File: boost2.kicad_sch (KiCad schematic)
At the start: 21 parts, among them IC1 CSD18543Q3A, IC2 LM3481QMMX_NOPB

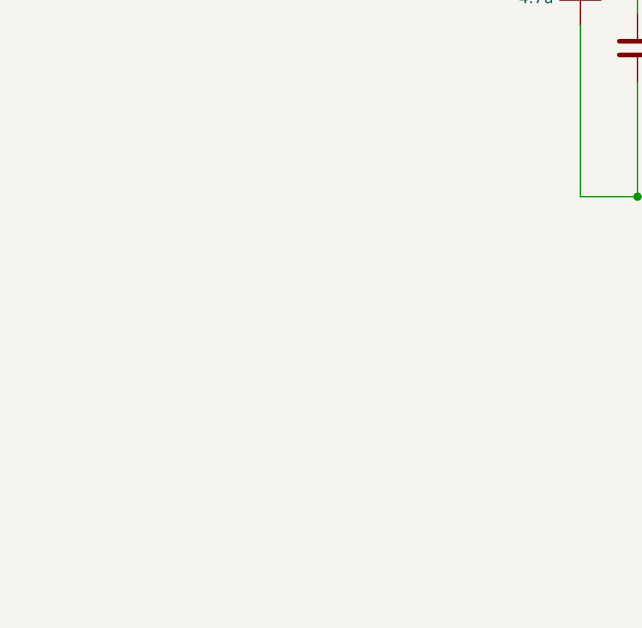
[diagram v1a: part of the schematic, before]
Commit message: Add new boost converter to boost2 subsheet
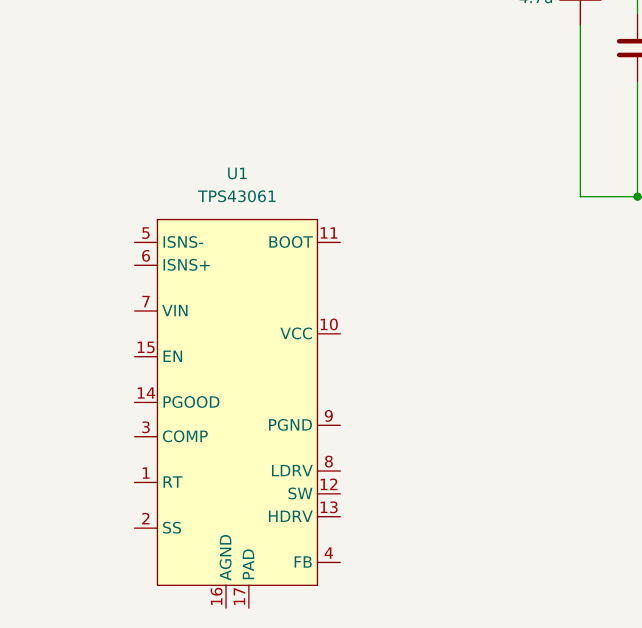
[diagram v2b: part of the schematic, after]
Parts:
- added U1: TPS43061, ! Robomaster ICs:Texas_S-PWQFN-N16, symbol ! Robomaster ICs:TPS43061
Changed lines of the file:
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@@
+	)
+	(symbol
+		(lib_id "! Robomaster ICs:TPS43061")
+		(at 48.26 138.43 0)
+		(unit 1)
+		(exclude_from_sim no)
+		(in_bom yes)
+		(on_board yes)
+		(dnp no)
+		(fields_autoplaced yes)
+		(property "Reference" "U1"
+			(at 48.26 133.35 0)
+			(effects
+				(font
+					(size 1.27 1.27)
+				)
+			)
+		)
+		(property "Value" "TPS43061"
+			(at 48.26 135.89 0)
+			(effects
+				(font
+					(size 1.27 1.27)
+				)
+			)
+		)
+		(property "Footprint" "! Robomaster ICs:Texas_S-PWQFN-N16"
+			(at 48.26 138.43 0)
+			(effects
+				(font
+					(size 1.27 1.27)
+				)
+				(hide yes)
+			)
+		)
+		(property "Datasheet" "https://www.ti.com/lit/ds/symlink/tps43061.pdf"
+			(at 48.26 138.43 0)
+			(effects
+				(font
+					(size 1.27 1.27)
+				)
+				(hide yes)
+			)
+		)
+		(property "Description" "Low Iq, Synchronous Boost Controller with Wide Input Voltage and 5.5V Gate Drive for Low Qg NexFETs"
+			(at 48.26 138.43 0)
+			(effects
+				(font
+					(size 1.27 1.27)
+				)
+				(hide yes)
+			)
+		)
+		(pin "11"
+		)
+		(pin "8"
+		)
+		(pin "12"
+		)
+		(pin "7"
+		)
+		(pin "6"
+		)
+		(pin "4"
+		)
+		(pin "13"
+		)
+		(pin "2"
+		)
+		(pin "16"
+		)
+		(pin "14"
+		)
+		(pin "17"
+		)
+		(pin "3"
+		)
+		(pin "9"
+		)
+		(pin "5"
+		)
+		(pin "10"
+		)
+		(pin "15"
+		)
+		(pin "1"
+		)
+		(instances
+			(project ""
+				(path "/6197145b-e7d4-44cc-9d90-537b6501bf60/47dffa6f-2678-4be2-969a-7f2e7310ccad"
+					(reference "U1")
+					(unit 1)
+				)
+			)
+		)
 	)
 	(symbol

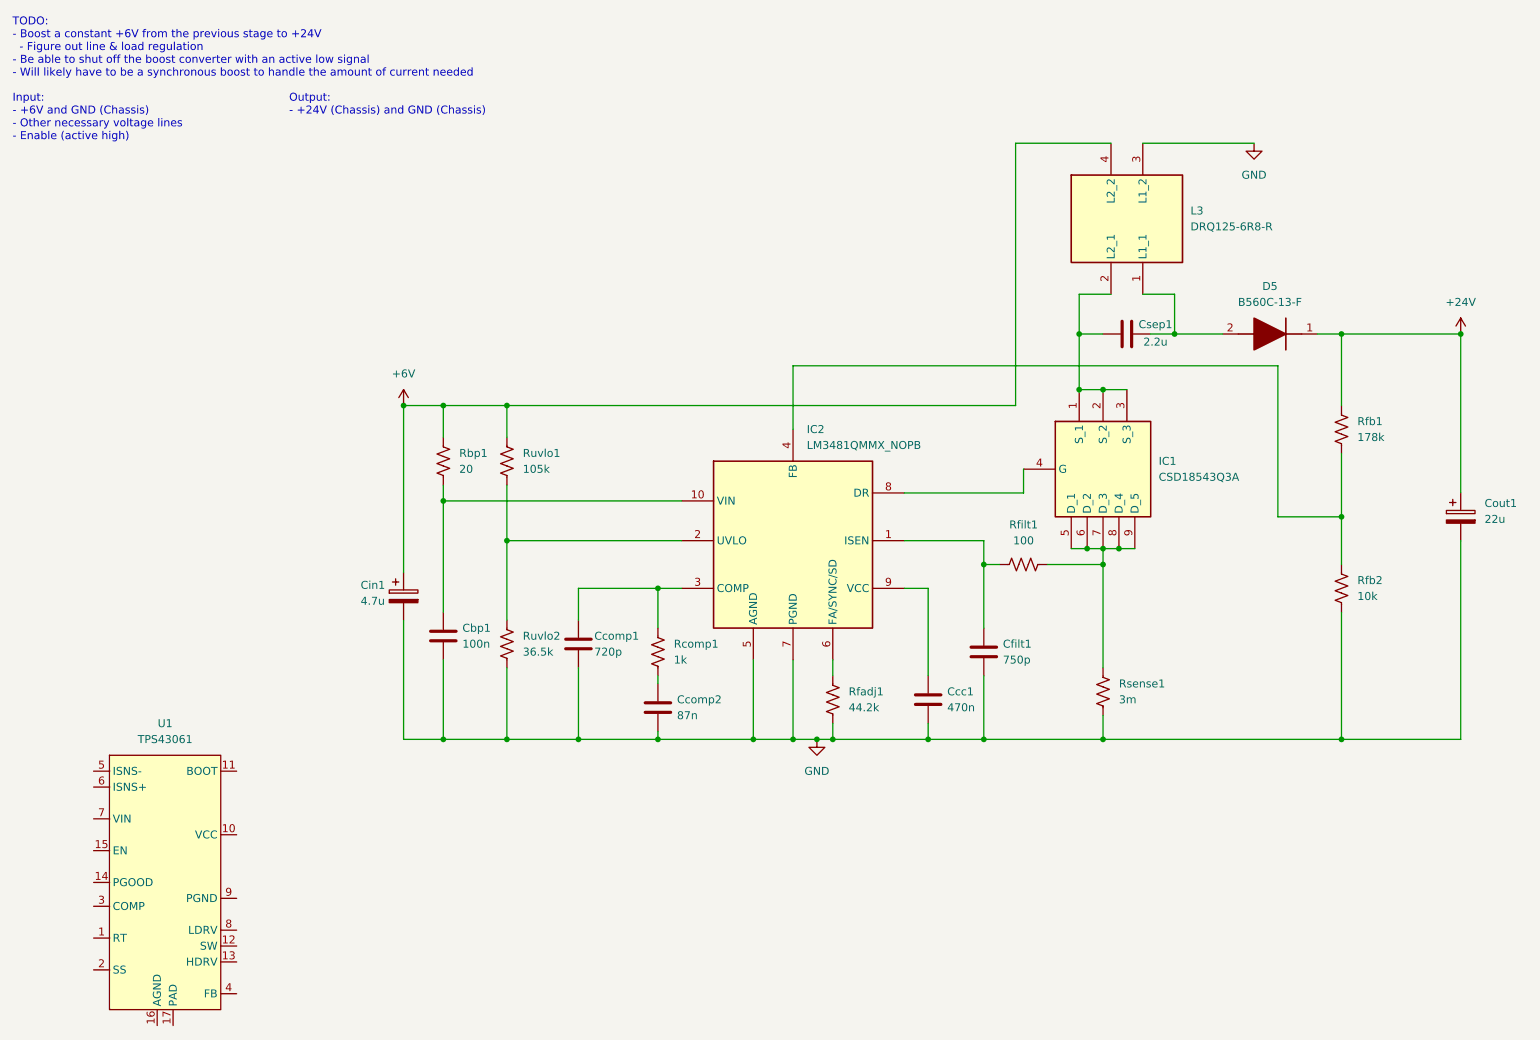
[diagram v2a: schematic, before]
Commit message: Completed stage 2 schematic
+ added SPICE models for all the custom components
+ renumbered components
+ updated library with stage 2 symbols
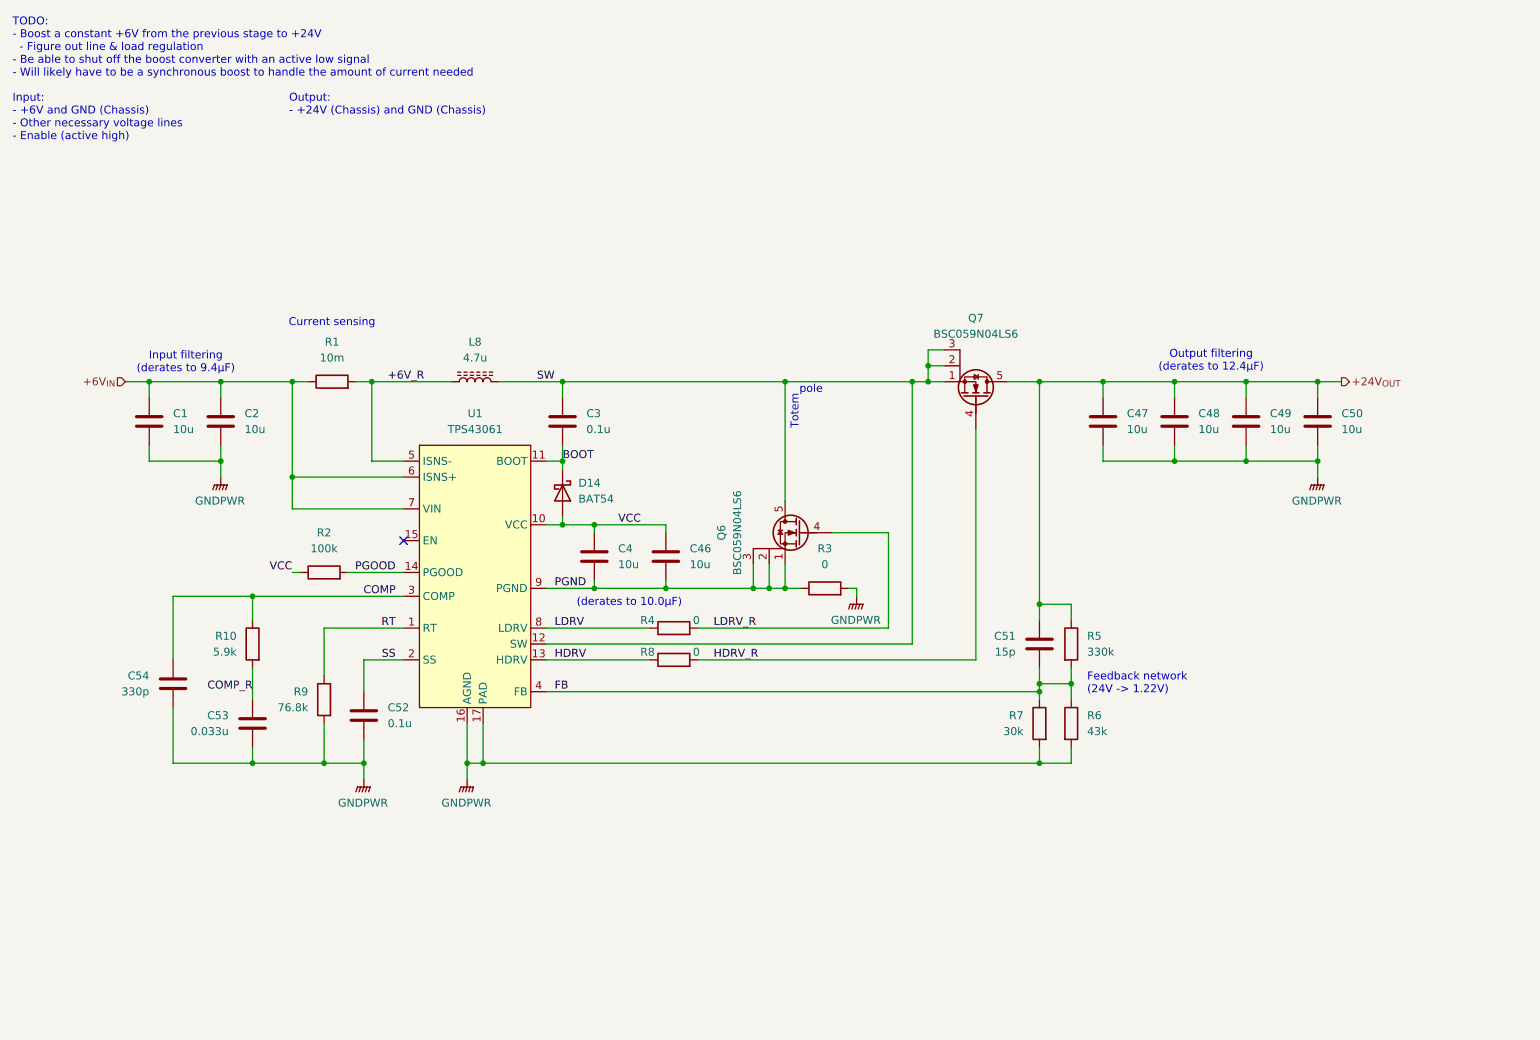
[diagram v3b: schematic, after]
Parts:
- removed Cbp1: 100n, symbol Device:C
- removed Ccc1: 470n, symbol Device:C
- removed Ccomp1: 720p, symbol Device:C
- removed Ccomp2: 87n, symbol Device:C
- removed Cfilt1: 750p, symbol Device:C
- removed Cin1: 4.7u, symbol Device:C_Polarized
- removed Cout1: 22u, symbol Device:C_Polarized
- removed Csep1: 2.2u, symbol Device:C
- removed D5: B560C-13-F, symbol boost2:B560C-13-F
- removed IC1: CSD18543Q3A, symbol boost2:CSD18543Q3A
- removed IC2: LM3481QMMX_NOPB, symbol boost2:LM3481QMMX_NOPB
- removed L3: DRQ125-6R8-R, symbol boost2:DRQ125-6R8-R
- removed Rbp1: 20, symbol Device:R_US
- removed Rcomp1: 1k, symbol Device:R_US
- removed Rfadj1: 44.2k, symbol Device:R_US
- removed Rfb1: 178k, symbol Device:R_US
- removed Rfb2: 10k, symbol Device:R_US
- removed Rfilt1: 100, symbol Device:R_US
- removed Rsense1: 3m, symbol Device:R_US
- removed Ruvlo1: 105k, symbol Device:R_US
- removed Ruvlo2: 36.5k, symbol Device:R_US
- added C1, C2, C4, C46: 10u, Capacitor_SMD:C_0805_2012Metric_Pad1.18x1.45mm_HandSolder, symbol Device:C
- added C3, C52: 0.1u, Capacitor_SMD:C_0603_1608Metric_Pad1.08x0.95mm_HandSolder, symbol Device:C
- added C47, C48, C49, C50: 10u, Capacitor_SMD:C_1206_3216Metric_Pad1.33x1.80mm_HandSolder, symbol Device:C
- added C51: 15p, Capacitor_SMD:C_0603_1608Metric_Pad1.08x0.95mm_HandSolder, symbol Device:C
- added C53: 0.033u, Capacitor_SMD:C_0603_1608Metric_Pad1.08x0.95mm_HandSolder, symbol Device:C
- added C54: 330p, Capacitor_SMD:C_0603_1608Metric_Pad1.08x0.95mm_HandSolder, symbol Device:C
- added D14: BAT54, Package_TO_SOT_SMD:SOT-23_Handsoldering, symbol Device:D_Schottky
- added L8: 4.7u, Inductor_SMD:L_Bourns_SRN8040TA, symbol Device:L_Ferrite
- added Q6, Q7: BSC059N04LS6, Package_SON:Infineon_PG-TDSON-8_6.15x5.15mm, symbol Transistor_FET:Q_NMOS_SGD
- added R1: 10m, Resistor_SMD:R_0612_1632Metric_Pad1.18x3.40mm_HandSolder, symbol Device:R
- added R10: 5.9k, Resistor_SMD:R_0603_1608Metric_Pad0.98x0.95mm_HandSolder, symbol Device:R
- added R2: 100k, Resistor_SMD:R_0603_1608Metric_Pad0.98x0.95mm_HandSolder, symbol Device:R
- added R3, R4, R8: 0, Resistor_SMD:R_0603_1608Metric_Pad0.98x0.95mm_HandSolder, symbol Device:R
- added R5: 330k, Resistor_SMD:R_0603_1608Metric_Pad0.98x0.95mm_HandSolder, symbol Device:R
- added R6: 43k, Resistor_SMD:R_0603_1608Metric_Pad0.98x0.95mm_HandSolder, symbol Device:R
- added R7: 30k, Resistor_SMD:R_0603_1608Metric_Pad0.98x0.95mm_HandSolder, symbol Device:R
- added R9: 76.8k, Resistor_SMD:R_0603_1608Metric_Pad0.98x0.95mm_HandSolder, symbol Device:R
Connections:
- net RT: now reaches U1.1 (RT)
- net RT: now also R9.1
- net VCC: now reaches U1.10 (VCC)
- net VCC: now also C4.1, C46.1, D14.1 (A), R2.1
- net BOOT: now reaches U1.11 (BOOT)
- net BOOT: now also C3.2, D14.3 (K)
- net SW: now reaches U1.12 (SW)
- net SW: now also C3.1, L8.2, Q6.5 (D), Q7.1 (S), Q7.2 (S), Q7.3 (S)
- net HDRV: now reaches U1.13 (HDRV)
- net HDRV: now also R8.1
- net PGOOD: now reaches U1.14 (PGOOD)
- net PGOOD: now also R2.2
- net GNDPWR: now reaches U1.16 (AGND)
- net GNDPWR: now also U1.17 (PAD), C1.2, C2.2, C47.2, C48.2, C49.2, C50.2, C52.2, C53.2, C54.2, R3.2, R6.2, R7.2, R9.2
- net SS: now reaches U1.2 (SS)
- net SS: now also C52.1
- net COMP: now reaches U1.3 (COMP)
- net COMP: now also C54.1, R10.1
- net FB: now reaches U1.4 (FB)
- net FB: now also C51.2, R5.2, R6.1, R7.1
- net +6V_R: now reaches U1.5 (ISNS-)
- net +6V_R: now also L8.1, R1.2
- net +6V_{IN}: now reaches U1.6 (ISNS+)
- net +6V_{IN}: now also U1.7 (VIN), C1.1, C2.1, R1.1
- net LDRV: now reaches U1.8 (LDRV)
- net LDRV: now also R4.1
- net PGND: now reaches U1.9 (PGND)
- net PGND: now also C4.2, C46.2, Q6.1 (S), Q6.2 (S), Q6.3 (S), R3.1
- new net +24V_{OUT}: C47.1, C48.1, C49.1, C50.1, C51.1, Q7.5 (D), R5.1
- new net COMP_R: C53.1, R10.2
- new net HDRV_R: Q7.4 (G), R8.2
- new net LDRV_R: Q6.4 (G), R4.2
- no-connect marks 0 -> 1
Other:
- note added: "(derates to 10.0µF)"
- note added: "Current sensing"
- note added: "Feedback network (24V -> 1.22V)"
- note added: "Input filtering (derates to 9.4µF)"
- note added: "Output filtering (derates to 12.4µF)"
- note added: "Totem"
- note added: "pole"
- moved on the sheet: U1

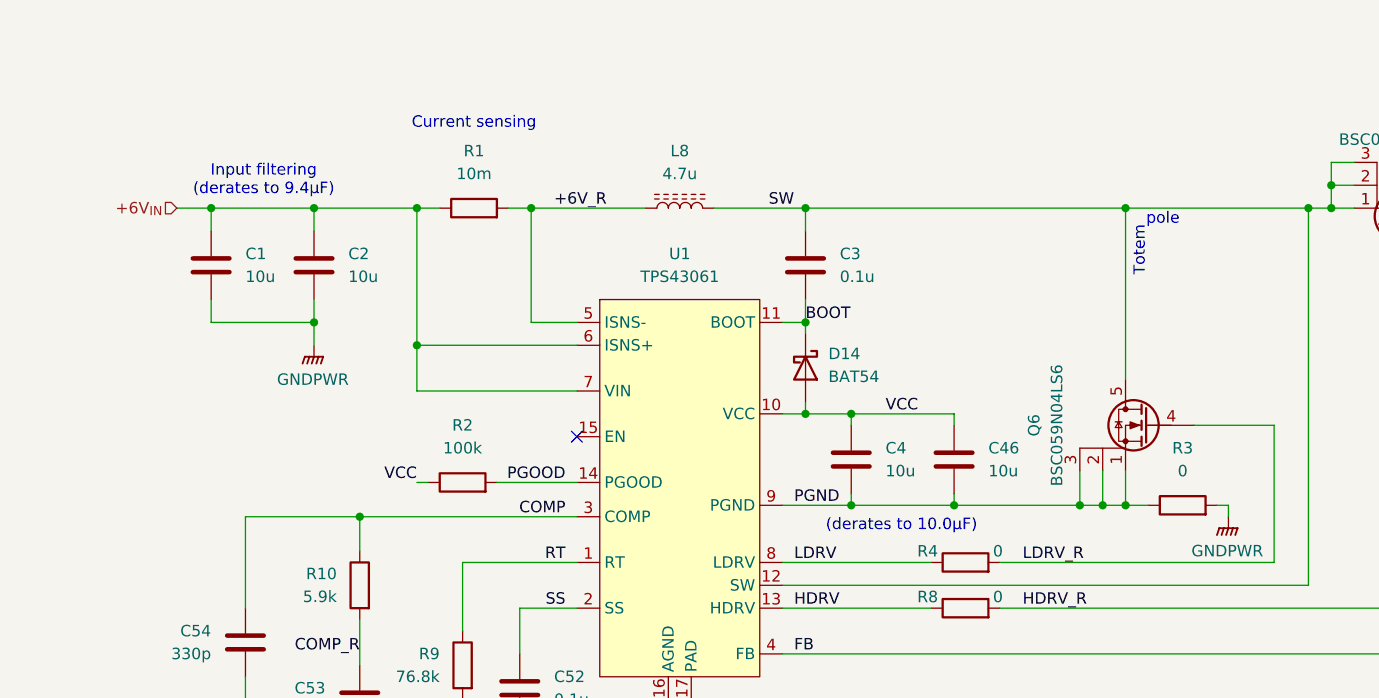
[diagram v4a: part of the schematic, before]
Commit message: Tuned circuits & adjusted values
Changed footprints for some circuits to consolidate components
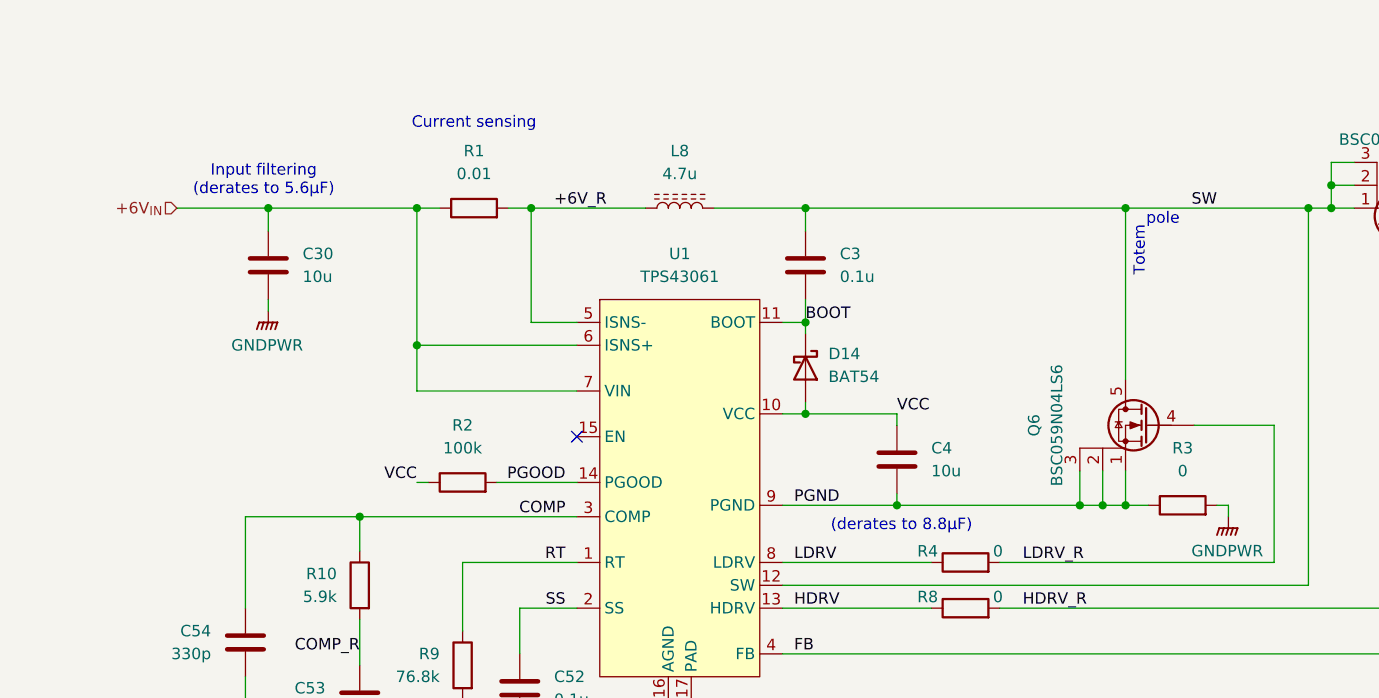
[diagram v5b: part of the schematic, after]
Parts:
- removed C1, C2, C46: 10u, Capacitor_SMD:C_0805_2012Metric_Pad1.18x1.45mm_HandSolder, symbol Device:C
- added C30: 10u, Capacitor_SMD:C_0805_2012Metric_Pad1.18x1.45mm_HandSolder, symbol Device:C
- R1: value 10m -> 0.01
- U1: Mouser Part Number (none) -> 595-TPS43061RTER
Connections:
- net +6V_{IN}: now also C30.1
- net GNDPWR: now also C30.2
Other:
- note added: "(derates to 8.8µF)"
- note added: "Input filtering (derates to 5.6µF)"
- note removed: "(derates to 10.0µF)"
- note removed: "Input filtering (derates to 9.4µF)"
- moved on the sheet: C4
